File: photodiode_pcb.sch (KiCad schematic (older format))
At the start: 15 parts, among them P1 CONN_01X04, U1 LTC2461, U3 SD100-13-23-222, U4 OPA381

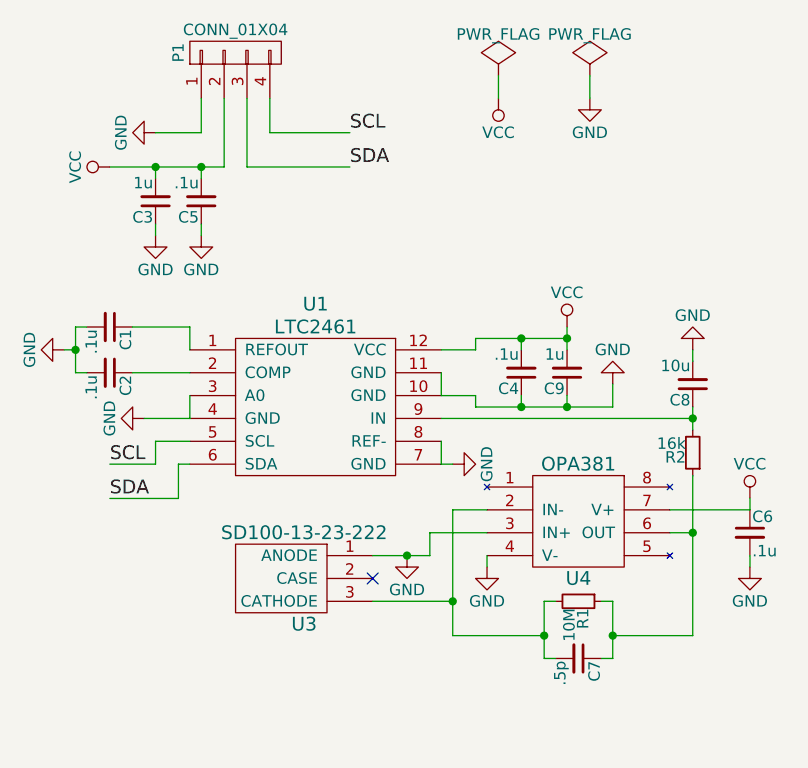
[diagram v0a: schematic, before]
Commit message: Reorganize pcb and change footprints
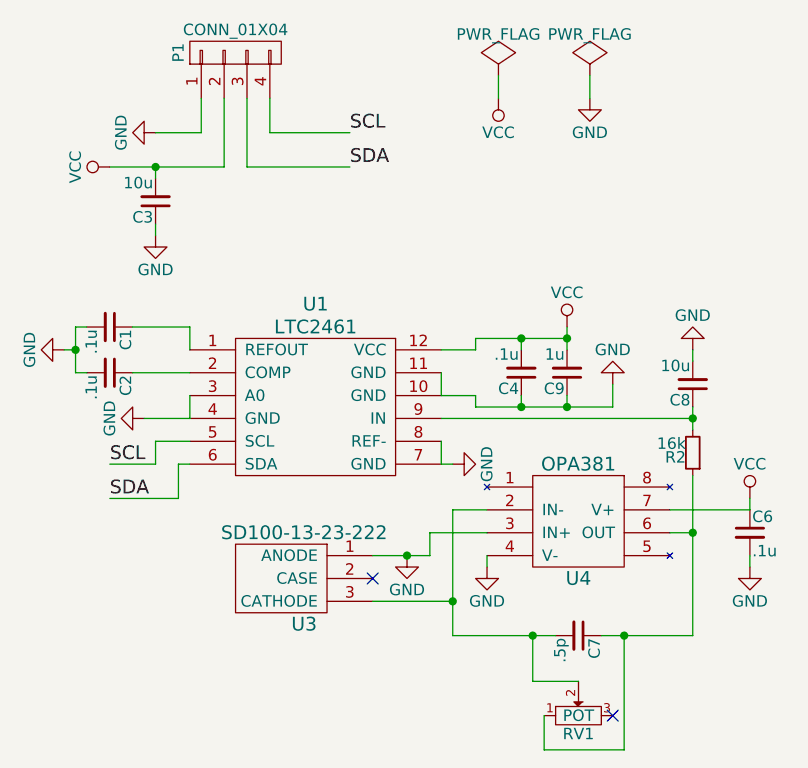
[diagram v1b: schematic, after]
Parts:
- removed C5: .1u, Capacitors_SMD:C_0603, symbol C_Small
- removed R1: 10M, footprints:R_0603_smaller_handsolder, symbol R_Small
- added RV1: POT, footprints:BOURNS_3214W, symbol POT
- C3: value 1u -> 10u
- P1: footprint Pin_Headers:Pin_Header_Straight_1x04 -> footprints:CONN_1x4_SMT_2mm
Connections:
- net at C7.2, U3.3 (CATHODE), U4.2 (IN-): now also RV1.2
- net at C7.1, R2.1, U4.6 (OUT): now also RV1.1
- no-connect marks 1 -> 2
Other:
- moved on the sheet: C7
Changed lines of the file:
@@
 LIBS:valves
 LIBS:rpi_absorbance
-LIBS:rpi_absorbance-cache
 EELAYER 25 0
 EELAYER END
@@
 $EndComp
 $Comp
-L C_Small C5
-U 1 1 56999F5A
-P 4600 2900
-F 0 "C5" H 4610 2970 50  0000 L CNN
-F 1 ".1u" H 4610 2820 50  0000 L CNN
-F 2 "Capacitors_SMD:C_0603" H 4600 2900 50  0001 C CNN
-F 3 "" H 4600 2900 50  0000 C CNN
-	1    4600 2900
-	-1   0    0    1
-$EndComp
-$Comp
-L GND #PWR01
-U 1 1 56999FB5
-P 4600 3050
-F 0 "#PWR01" H 4600 2800 50  0001 C CNN
-F 1 "GND" H 4600 2900 50  0000 C CNN
-F 2 "" H 4600 3050 50  0000 C CNN
-F 3 "" H 4600 3050 50  0000 C CNN
-	1    4600 3050
-	1    0    0    -1
-$EndComp
-$Comp
 L C_Small C3
 U 1 1 569ABE13
 P 4400 2900
 F 0 "C3" H 4410 2970 50  0000 L CNN
-F 1 "1u" H 4410 2820 50  0000 L CNN
+F 1 "10u" H 4410 2820 50  0000 L CNN
 F 2 "Capacitors_SMD:C_0603" H 4400 2900 50  0001 C CNN
 F 3 "" H 4400 2900 50  0000 C CNN
@@
 $EndComp
 $Comp
-L GND #PWR02
+L GND #PWR01
 U 1 1 569AD39F
 P 4400 3050
-F 0 "#PWR02" H 4400 2800 50  0001 C CNN
+F 0 "#PWR01" H 4400 2800 50  0001 C CNN
 F 1 "GND" H 4400 2900 50  0000 C CNN
 F 2 "" H 4400 3050 50  0000 C CNN
@@
 $EndComp
 $Comp
-L GND #PWR03
+L GND #PWR02
 U 1 1 569AE178
 P 4400 2600
-F 0 "#PWR03" H 4400 2350 50  0001 C CNN
+F 0 "#PWR02" H 4400 2350 50  0001 C CNN
 F 1 "GND" H 4400 2450 50  0000 C CNN
 F 2 "" H 4400 2600 50  0000 C CNN
@@
 $EndComp
 $Comp
-L VCC #PWR04
+L VCC #PWR03
 U 1 1 569AF392
 P 7000 4200
-F 0 "#PWR04" H 7000 4050 50  0001 C CNN
+F 0 "#PWR03" H 7000 4050 50  0001 C CNN
 F 1 "VCC" H 7000 4350 50  0000 C CNN
 F 2 "" H 7000 4200 50  0000 C CNN
@@
 $EndComp
 $Comp
-L GND #PWR05
+L GND #PWR04
 U 1 1 569AF4AF
 P 7000 4500
-F 0 "#PWR05" H 7000 4250 50  0001 C CNN
+F 0 "#PWR04" H 7000 4250 50  0001 C CNN
 F 1 "GND" H 7000 4350 50  0000 C CNN
 F 2 "" H 7000 4500 50  0000 C CNN
@@
 $EndComp
 $Comp
-L GND #PWR06
+L GND #PWR05
 U 1 1 569AF99E
 P 5500 4450
-F 0 "#PWR06" H 5500 4200 50  0001 C CNN
+F 0 "#PWR05" H 5500 4200 50  0001 C CNN
 F 1 "GND" H 5500 4300 50  0000 C CNN
 F 2 "" H 5500 4450 50  0000 C CNN
@@
 $EndComp
 $Comp
-L VCC #PWR07
+L VCC #PWR06
 U 1 1 569AFDE2
 P 4200 2750
-F 0 "#PWR07" H 4200 2600 50  0001 C CNN
+F 0 "#PWR06" H 4200 2600 50  0001 C CNN
 F 1 "VCC" H 4200 2900 50  0000 C CNN
 F 2 "" H 4200 2750 50  0000 C CNN
@@
 $EndComp
 $Comp
-L GND #PWR08
+L GND #PWR07
 U 1 1 569B1CCA
 P 5850 4500
-F 0 "#PWR08" H 5850 4250 50  0001 C CNN
+F 0 "#PWR07" H 5850 4250 50  0001 C CNN
 F 1 "GND" H 5850 4350 50  0000 C CNN
 F 2 "" H 5850 4500 50  0000 C CNN
@@
 L C_Small C7
 U 1 1 569B2162
-P 6250 4900
-F 0 "C7" H 6260 4970 50  0000 L CNN
-F 1 ".5p" H 6260 4820 50  0000 L CNN
-F 2 "Capacitors_SMD:C_0603" H 6250 4900 50  0001 C CNN
-F 3 "" H 6250 4900 50  0000 C CNN
-	1    6250 4900
-	0    1    1    0
-$EndComp
-$Comp
-L R_Small R1
-U 1 1 569B21BE
-P 6250 4650
-F 0 "R1" H 6280 4670 50  0000 L CNN
-F 1 "10M" H 6280 4610 50  0000 L CNN
-F 2 "footprints:R_0603_smaller_handsolder" H 6250 4650 50  0001 C CNN
-F 3 "" H 6250 4650 50  0000 C CNN
-	1    6250 4650
+P 6250 4800
+F 0 "C7" H 6260 4870 50  0000 L CNN
+F 1 ".5p" H 6260 4720 50  0000 L CNN
+F 2 "Capacitors_SMD:C_0603" H 6250 4800 50  0001 C CNN
+F 3 "" H 6250 4800 50  0000 C CNN
+	1    6250 4800
 	0    1    1    0
 $EndComp
@@
 $EndComp
 $Comp
-L GND #PWR09
+L GND #PWR08
 U 1 1 569B3249
 P 6750 3550
-F 0 "#PWR09" H 6750 3300 50  0001 C CNN
+F 0 "#PWR08" H 6750 3300 50  0001 C CNN
 F 1 "GND" H 6750 3400 50  0000 C CNN
 F 2 "" H 6750 3550 50  0000 C CNN
@@
 $EndComp
 $Comp
-L GND #PWR010
+L GND #PWR09
 U 1 1 569C0022
 P 4000 3550
-F 0 "#PWR010" H 4000 3300 50  0001 C CNN
+F 0 "#PWR09" H 4000 3300 50  0001 C CNN
 F 1 "GND" H 4000 3400 50  0000 C CNN
 F 2 "" H 4000 3550 50  0000 C CNN
@@
 $EndComp
 $Comp
-L GND #PWR011
+L GND #PWR010
 U 1 1 569C085F
 P 6400 3700
-F 0 "#PWR011" H 6400 3450 50  0001 C CNN
+F 0 "#PWR010" H 6400 3450 50  0001 C CNN
 F 1 "GND" H 6400 3550 50  0000 C CNN
 F 2 "" H 6400 3700 50  0000 C CNN
@@
 $EndComp
 $Comp
-L GND #PWR012
+L GND #PWR011
 U 1 1 569C0987
 P 5700 4050
-F 0 "#PWR012" H 5700 3800 50  0001 C CNN
+F 0 "#PWR011" H 5700 3800 50  0001 C CNN
 F 1 "GND" H 5700 3900 50  0000 C CNN
 F 2 "" H 5700 4050 50  0000 C CNN
@@
 $EndComp
 $Comp
-L VCC #PWR013
+L VCC #PWR012
 U 1 1 569C1370
 P 6200 3450
-F 0 "#PWR013" H 6200 3300 50  0001 C CNN
+F 0 "#PWR012" H 6200 3300 50  0001 C CNN
 F 1 "VCC" H 6200 3600 50  0000 C CNN
 F 2 "" H 6200 3450 50  0000 C CNN
@@
 $EndComp
 $Comp
-L GND #PWR014
+L GND #PWR013
 U 1 1 569C17EB
 P 4350 3850
-F 0 "#PWR014" H 4350 3600 50  0001 C CNN
+F 0 "#PWR013" H 4350 3600 50  0001 C CNN
 F 1 "GND" H 4350 3700 50  0000 C CNN
 F 2 "" H 4350 3850 50  0000 C CNN
@@
 	6750 3800 6750 3900
 Wire Wire Line
-	6750 4100 6750 4800
+	6750 4800 6750 4100
 Wire Wire Line
 	4550 3450 4300 3450
@@
 Wire Wire Line
 	6750 3550 6750 3600
-Connection ~ 6400 4800
 Connection ~ 6750 4350
 Wire Wire Line
-	6750 4800 6400 4800
-Wire Wire Line
-	6400 4900 6350 4900
-Wire Wire Line
-	6400 4650 6400 4900
-Wire Wire Line
-	6350 4650 6400 4650
-Connection ~ 6100 4800
-Wire Wire Line
-	6100 4900 6150 4900
+	6350 4800 6750 4800
 Connection ~ 5700 4650
 Wire Wire Line
-	6100 4650 6150 4650
-Wire Wire Line
-	6100 4650 6100 4900
-Wire Wire Line
-	5700 4800 6100 4800
+	5700 4800 6150 4800
 Wire Wire Line
 	5850 4500 5850 4450
@@
 Wire Wire Line
 	4400 3000 4400 3050
-Wire Wire Line
-	4600 3050 4600 3000
 NoConn ~ 5350 4550
 $Comp
@@
 F 0 "P1" H 4750 2500 50  0000 C CNN
 F 1 "CONN_01X04" V 4850 2250 50  0000 C CNN
-F 2 "Pin_Headers:Pin_Header_Straight_1x04" H 4750 2250 50  0001 C CNN
+F 2 "footprints:CONN_1x4_SMT_2mm" H 4750 2250 50  0001 C CNN
 F 3 "" H 4750 2250 50  0000 C CNN
 	1    4750 2250
@@
 	4700 2750 4700 2450
 Wire Wire Line
-	4600 2800 4600 2750
-Connection ~ 4600 2750
-Wire Wire Line
 	4800 2450 4800 2750
 Wire Wire Line
@@
 SCL
 $Comp
-L PWR_FLAG #FLG015
+L PWR_FLAG #FLG014
 U 1 1 56AD25FD
 P 5900 2350
-F 0 "#FLG015" H 5900 2445 50  0001 C CNN
+F 0 "#FLG014" H 5900 2445 50  0001 C CNN
 F 1 "PWR_FLAG" H 5900 2530 50  0000 C CNN
 F 2 "" H 5900 2350 50  0000 C CNN
@@
 $EndComp
 $Comp
-L PWR_FLAG #FLG016
+L PWR_FLAG #FLG015
 U 1 1 56AD2653
 P 6300 2350
-F 0 "#FLG016" H 6300 2445 50  0001 C CNN
+F 0 "#FLG015" H 6300 2445 50  0001 C CNN
 F 1 "PWR_FLAG" H 6300 2530 50  0000 C CNN
 F 2 "" H 6300 2350 50  0000 C CNN
@@
 $EndComp
 $Comp
-L VCC #PWR017
+L VCC #PWR016
 U 1 1 56AD2682
 P 5900 2450
-F 0 "#PWR017" H 5900 2300 50  0001 C CNN
+F 0 "#PWR016" H 5900 2300 50  0001 C CNN
 F 1 "VCC" H 5900 2600 50  0000 C CNN
 F 2 "" H 5900 2450 50  0000 C CNN
@@
 	5900 2350 5900 2450
 $Comp
-L GND #PWR018
+L GND #PWR017
 U 1 1 56AD2722
 P 6300 2450
-F 0 "#PWR018" H 6300 2200 50  0001 C CNN
+F 0 "#PWR017" H 6300 2200 50  0001 C CNN
 F 1 "GND" H 6300 2300 50  0000 C CNN
 F 2 "" H 6300 2450 50  0000 C CNN
@@
 Wire Wire Line
 	6300 2450 6300 2350
+$Comp
+L POT RV1
+U 1 1 56D7CCFF
+P 6250 5150
+F 0 "RV1" H 6250 5070 50  0000 C CNN
+F 1 "POT" H 6250 5150 50  0000 C CNN
+F 2 "footprints:BOURNS_3214W" H 6250 5150 50  0001 C CNN
+F 3 "" H 6250 5150 50  0000 C CNN
+	1    6250 5150
+	1    0    0    -1
+$EndComp
+Wire Wire Line
+	6250 5000 6050 5000
+Wire Wire Line
+	6050 5000 6050 4800
+Connection ~ 6050 4800
+Connection ~ 6450 4800
+Wire Wire Line
+	6450 4800 6450 5300
+Wire Wire Line
+	6450 5300 6100 5300
+Wire Wire Line
+	6100 5300 6100 5150
+NoConn ~ 6400 5150
 $EndSCHEMATC

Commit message: Reorganize project
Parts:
- P1: footprint footprints:CONN_1x4_SMT_2mm -> jnod_footprints:Sullins_M89_1X4
- R2: footprint footprints:R_0603_smaller_handsolder -> jnod_footprints:R_0603_smaller_handsolder
- RV1: value POT -> 2M; footprint footprints:BOURNS_3214W -> jnod_footprints:BOURNS_3214W
- U3: footprint footprints:SD100-13-23-222 -> jnod_footprints:TO-5-3
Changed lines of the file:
@@
 LIBS:valves
 LIBS:rpi_absorbance
+LIBS:photodiode_pcb-cache
 EELAYER 25 0
 EELAYER END
@@
 F 0 "U3" H 5050 3850 60  0000 C CNN
 F 1 "SD100-13-23-222" H 5050 4250 60  0000 C CNN
-F 2 "footprints:SD100-13-23-222" H 5100 4300 60  0001 C CNN
+F 2 "jnod_footprints:TO-5-3" H 5100 4300 60  0001 C CNN
 F 3 "" H 5100 4300 60  0000 C CNN
 	1    5100 4300
@@
 F 0 "R2" H 6780 4020 50  0000 L CNN
 F 1 "16k" H 6780 3960 50  0000 L CNN
-F 2 "footprints:R_0603_smaller_handsolder" H 6750 4000 50  0001 C CNN
+F 2 "jnod_footprints:R_0603_smaller_handsolder" H 6750 4000 50  0001 C CNN
 F 3 "" H 6750 4000 50  0000 C CNN
 	1    6750 4000
@@
 F 0 "P1" H 4750 2500 50  0000 C CNN
 F 1 "CONN_01X04" V 4850 2250 50  0000 C CNN
-F 2 "footprints:CONN_1x4_SMT_2mm" H 4750 2250 50  0001 C CNN
+F 2 "jnod_footprints:Sullins_M89_1X4" H 4750 2250 50  0001 C CNN
 F 3 "" H 4750 2250 50  0000 C CNN
 	1    4750 2250
@@
 P 6250 5150
 F 0 "RV1" H 6250 5070 50  0000 C CNN
-F 1 "POT" H 6250 5150 50  0000 C CNN
-F 2 "footprints:BOURNS_3214W" H 6250 5150 50  0001 C CNN
+F 1 "2M" H 6250 5150 50  0000 C CNN
+F 2 "jnod_footprints:BOURNS_3214W" H 6250 5150 50  0001 C CNN
 F 3 "" H 6250 5150 50  0000 C CNN
 	1    6250 5150

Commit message: Update silk screen
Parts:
- R2: footprint jnod_footprints:R_0603_smaller_handsolder -> Resistors_SMD:R_0603
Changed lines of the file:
@@
 F 0 "R2" H 6780 4020 50  0000 L CNN
 F 1 "16k" H 6780 3960 50  0000 L CNN
-F 2 "jnod_footprints:R_0603_smaller_handsolder" H 6750 4000 50  0001 C CNN
+F 2 "Resistors_SMD:R_0603" H 6750 4000 50  0001 C CNN
 F 3 "" H 6750 4000 50  0000 C CNN
 	1    6750 4000
